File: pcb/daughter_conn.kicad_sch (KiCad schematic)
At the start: 0 parts

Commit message: moved stuff around
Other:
- note added: "26 pins, and maybe some extra grounds"
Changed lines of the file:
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@@
 	(generator_version "10.0")
 	(paper "A5")
+	(text "26 pins, and maybe some extra grounds"
+		(exclude_from_sim no)
+		(at 119.38 62.992 0)
+		(effects
+			(font
+				(size 1.27 1.27)
+			)
+		)
+	)
 	(text "i2c1, spi0, uart0"
 		(exclude_from_sim no)
@@
 	(wire
 		(pts
+			(xy 130.81 41.91) (xy 132.08 41.91)
+		)
+		(stroke
+			(width 0)
+			(type default)
+		)
+	)
+	(wire
+		(pts
 			(xy 154.94 39.37) (xy 168.91 39.37)
 		)
@@
 		(pts
 			(xy 171.45 40.64) (xy 171.45 17.78)
+		)
+		(stroke
+			(width 0)
+			(type default)
+		)
+	)
+	(wire
+		(pts
+			(xy 130.81 44.45) (xy 132.08 44.45)
 		)
 		(stroke
@@
 	)
 	(hierarchical_label "mod2{DET}"
-		(shape input)
+		(shape bidirectional)
 		(at 133.35 17.78 0)
 		(effects
@@
 		)
 	)
+	(hierarchical_label "GND"
+		(shape bidirectional)
+		(at 132.08 44.45 0)
+		(effects
+			(font
+				(size 1.27 1.27)
+			)
+			(justify left)
+		)
+	)
 	(hierarchical_label "mod3{DET}"
-		(shape input)
+		(shape bidirectional)
 		(at 133.35 25.4 0)
 		(effects
@@
 		)
 	)
+	(hierarchical_label "+3V3"
+		(shape input)
+		(at 132.08 41.91 0)
+		(effects
+			(font
+				(size 1.27 1.27)
+			)
+			(justify left)
+		)
+	)
+	(symbol
+		(lib_name "+3V3_1")
+		(lib_id "power:+3V3")
+		(at 130.81 41.91 0)
+		(unit 1)
+		(body_style 1)
+		(exclude_from_sim no)
+		(in_bom yes)
+		(on_board yes)
+		(in_pos_files yes)
+		(dnp no)
+		(property "Reference" "#PWR095"
+			(at 130.81 45.72 0)
+			(hide yes)
+			(show_name no)
+			(do_not_autoplace no)
+			(effects
+				(font
+					(size 1.27 1.27)
+				)
+			)
+		)
+		(property "Value" "+3V3"
+			(at 127.254 40.64 0)
+			(show_name no)
+			(do_not_autoplace no)
+			(effects
+				(font
+					(size 1.27 1.27)
+				)
+			)
+		)
+		(property "Footprint" ""
+			(at 130.81 41.91 0)
+			(hide yes)
+			(show_name no)
+			(do_not_autoplace no)
+			(effects
+				(font
+					(size 1.27 1.27)
+				)
+			)
+		)
+		(property "Datasheet" ""
+			(at 130.81 41.91 0)
+			(hide yes)
+			(show_name no)
+			(do_not_autoplace no)
+			(effects
+				(font
+					(size 1.27 1.27)
+				)
+			)
+		)
+		(property "Description" "Power symbol creates a global label with name \"+3V3\""
+			(at 130.81 41.91 0)
+			(hide yes)
+			(show_name no)
+			(do_not_autoplace no)
+			(effects
+				(font
+					(size 1.27 1.27)
+				)
+			)
+		)
+		(pin "1"
+		)
+		(instances
+			(project "hackxpansion"
+				(path "/aaf5804d-3f78-442b-969e-39faa388db94/3ee99963-5fb2-4fd0-b832-3d641b7ff03c"
+					(reference "#PWR095")
+					(unit 1)
+				)
+				(path "/aaf5804d-3f78-442b-969e-39faa388db94/5128c8bf-7fd5-4142-8f5c-357a729d9a97"
+					(reference "#PWR079")
+					(unit 1)
+				)
+			)
+		)
+	)
+	(symbol
+		(lib_id "power:GND")
+		(at 130.81 44.45 0)
+		(mirror y)
+		(unit 1)
+		(body_style 1)
+		(exclude_from_sim no)
+		(in_bom yes)
+		(on_board yes)
+		(in_pos_files yes)
+		(dnp no)
+		(property "Reference" "#PWR096"
+			(at 130.81 50.8 0)
+			(hide yes)
+			(show_name no)
+			(do_not_autoplace no)
+			(effects
+				(font
+					(size 1.27 1.27)
+				)
+			)
+		)
+		(property "Value" "GND"
+			(at 126.746 46.228 0)
+			(show_name no)
+			(do_not_autoplace no)
+			(effects
+				(font
+					(size 1.27 1.27)
+				)
+			)
+		)
+		(property "Footprint" ""
+			(at 130.81 44.45 0)
+			(hide yes)
+			(show_name no)
+			(do_not_autoplace no)
+			(effects
+				(font
+					(size 1.27 1.27)
+				)
+			)
+		)
+		(property "Datasheet" ""
+			(at 130.81 44.45 0)
+			(hide yes)
+			(show_name no)
+			(do_not_autoplace no)
+			(effects
+				(font
+					(size 1.27 1.27)
+				)
+			)
+		)
+		(property "Description" "Power symbol creates a global label with name \"GND\" , ground"
+			(at 130.81 44.45 0)
+			(hide yes)
+			(show_name no)
+			(do_not_autoplace no)
+			(effects
+				(font
+					(size 1.27 1.27)
+				)
+			)
+		)
+		(pin "1"
+		)
+		(instances
+			(project "hackxpansion"
+				(path "/aaf5804d-3f78-442b-969e-39faa388db94/3ee99963-5fb2-4fd0-b832-3d641b7ff03c"
+					(reference "#PWR096")
+					(unit 1)
+				)
+				(path "/aaf5804d-3f78-442b-969e-39faa388db94/5128c8bf-7fd5-4142-8f5c-357a729d9a97"
+					(reference "#PWR080")
+					(unit 1)
+				)
+			)
+		)
+	)

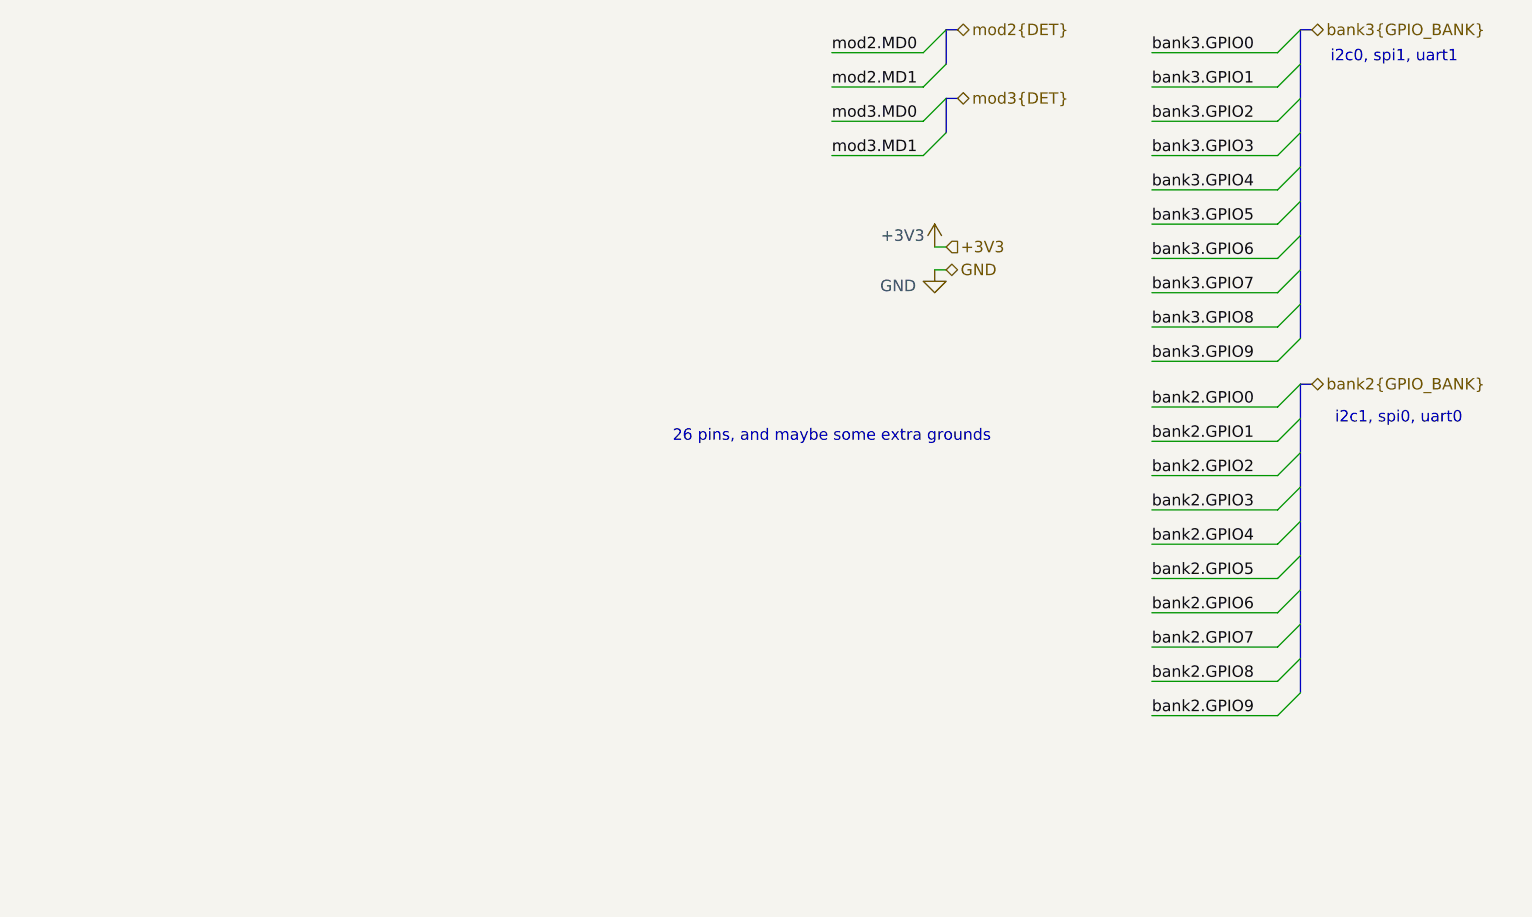
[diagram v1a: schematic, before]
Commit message: finished rough schematic
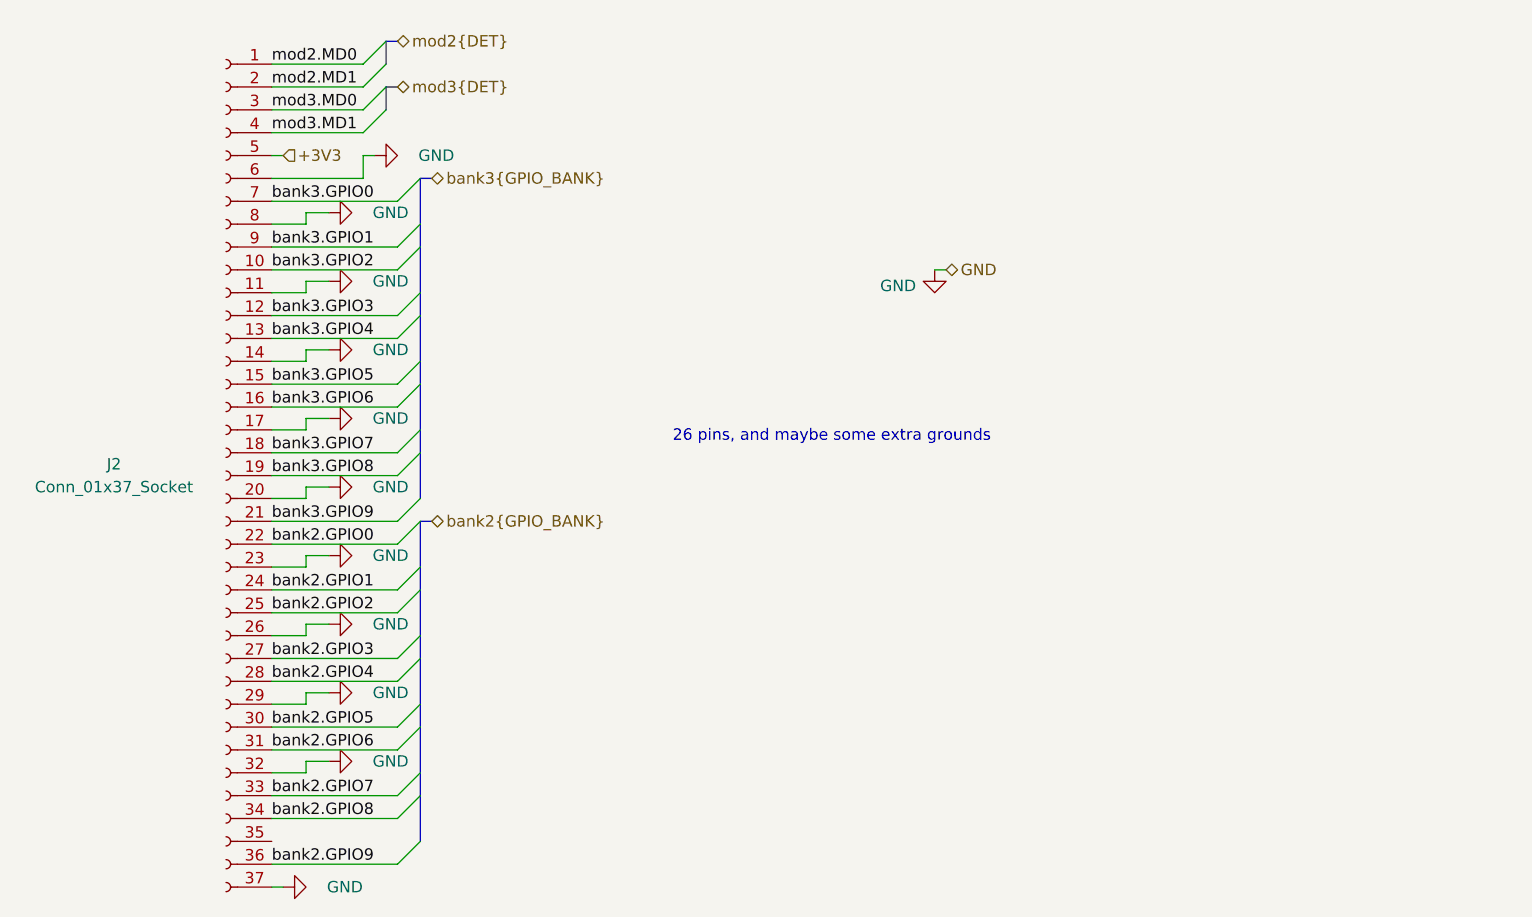
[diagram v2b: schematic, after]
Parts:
- added J2: Conn_01x37_Socket, symbol Connector:Conn_01x37_Socket
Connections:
- net +3V3: now also J2.5 (Pin_5)
- net GND: now also J2.11 (Pin_11), J2.14 (Pin_14), J2.17 (Pin_17), J2.20 (Pin_20), J2.23 (Pin_23), J2.26 (Pin_26), J2.29 (Pin_29), J2.32 (Pin_32), J2.37 (Pin_37), J2.6 (Pin_6), J2.8 (Pin_8)
- net bank2.GPIO0: now also J2.22 (Pin_22)
- net bank2.GPIO1: now also J2.24 (Pin_24)
- net bank2.GPIO2: now also J2.25 (Pin_25)
- net bank2.GPIO3: now also J2.27 (Pin_27)
- net bank2.GPIO4: now also J2.28 (Pin_28)
- net bank2.GPIO5: now also J2.30 (Pin_30)
- net bank2.GPIO6: now also J2.31 (Pin_31)
- net bank2.GPIO7: now also J2.33 (Pin_33)
- net bank2.GPIO8: now also J2.34 (Pin_34)
- net bank2.GPIO9: now also J2.36 (Pin_36)
- net bank3.GPIO0: now also J2.7 (Pin_7)
- net bank3.GPIO1: now also J2.9 (Pin_9)
- net bank3.GPIO2: now also J2.10 (Pin_10)
- net bank3.GPIO3: now also J2.12 (Pin_12)
- net bank3.GPIO4: now also J2.13 (Pin_13)
- net bank3.GPIO5: now also J2.15 (Pin_15)
- net bank3.GPIO6: now also J2.16 (Pin_16)
- net bank3.GPIO7: now also J2.18 (Pin_18)
- net bank3.GPIO8: now also J2.19 (Pin_19)
- net bank3.GPIO9: now also J2.21 (Pin_21)
- net mod2.MD0: now also J2.1 (Pin_1)
- net mod2.MD1: now also J2.2 (Pin_2)
- net mod3.MD0: now also J2.3 (Pin_3)
- net mod3.MD1: now also J2.4 (Pin_4)
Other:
- note removed: "i2c0, spi1, uart1"
- note removed: "i2c1, spi0, uart0"

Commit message: switched to pico blade connectors
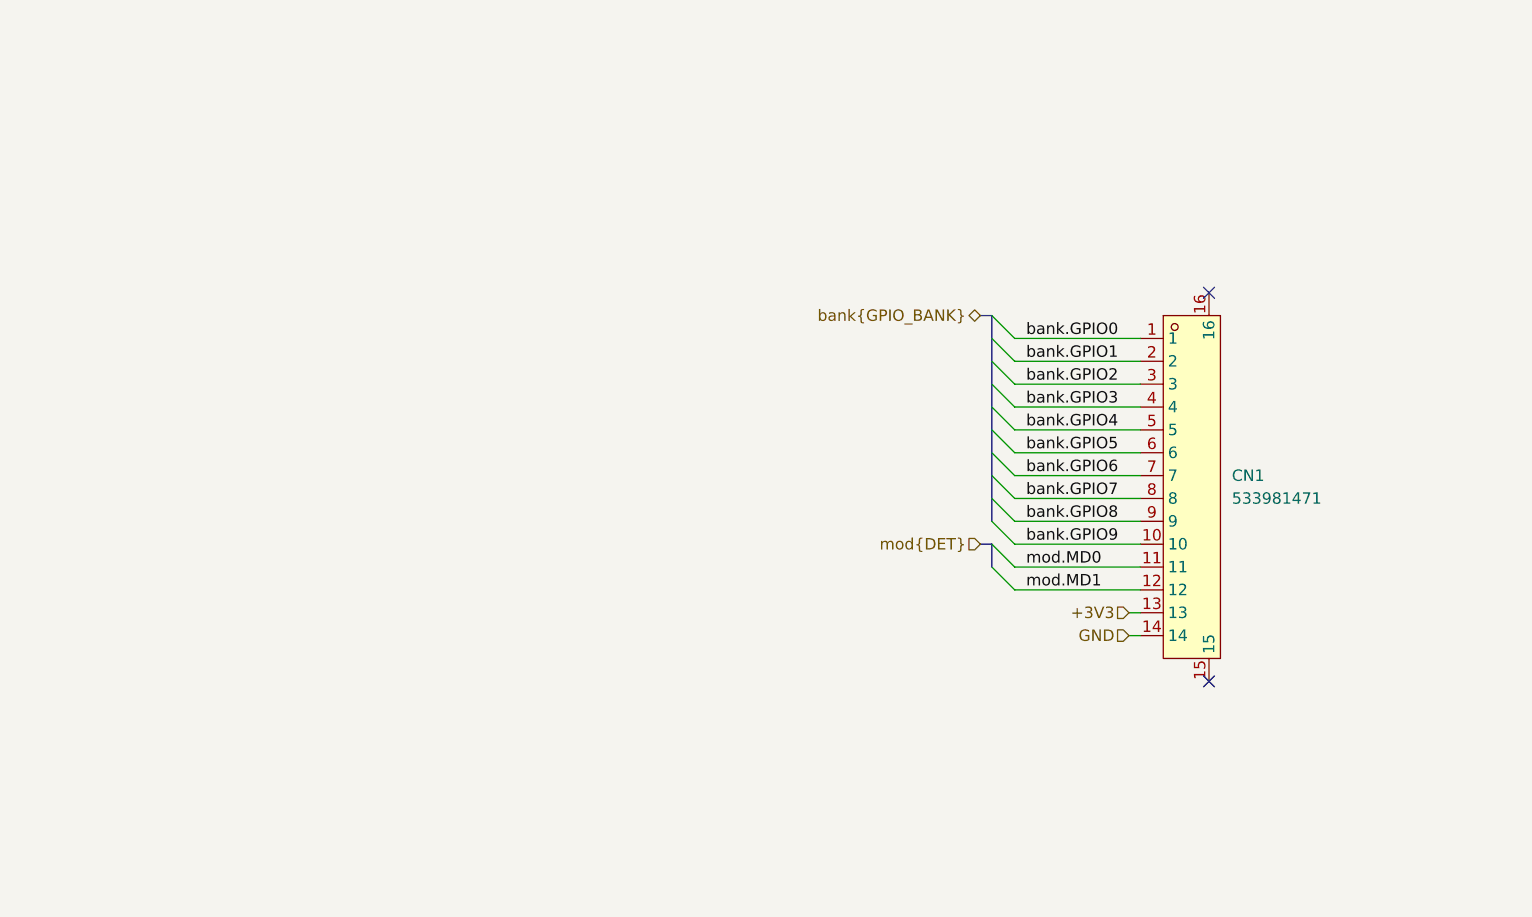
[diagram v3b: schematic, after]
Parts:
- removed J2: Conn_01x37_Socket, symbol Connector:Conn_01x37_Socket
- added CN1: 533981471, easyeda2kicad:CONN-SMD_14P-P1.25_MOLEX_533981471, symbol easyeda2kicad:533981471
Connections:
- net +3V3: now also CN1.13
- net GND: now also CN1.14
- new net bank.GPIO0: CN1.1
- new net bank.GPIO1: CN1.2
- new net bank.GPIO2: CN1.3
- new net bank.GPIO3: CN1.4
- new net bank.GPIO4: CN1.5
- new net bank.GPIO5: CN1.6
- new net bank.GPIO6: CN1.7
- new net bank.GPIO7: CN1.8
- new net bank.GPIO8: CN1.9
- new net bank.GPIO9: CN1.10
- new net mod.MD0: CN1.11
- new net mod.MD1: CN1.12
- no-connect marks 0 -> 2
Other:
- note removed: "26 pins, and maybe some extra grounds"

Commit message: finished basic routing
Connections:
- net GND: now also CN1.15, CN1.16
- no-connect marks 2 -> 0
